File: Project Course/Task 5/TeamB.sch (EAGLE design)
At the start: 33 parts, among them Q1 MIC29300-5.0WU, Q2 MIC29300-3.3WU, Q3 MIC29300-12WU, U0 26V, U1 26V, U2 5V, U3 3.3V, U4 12V

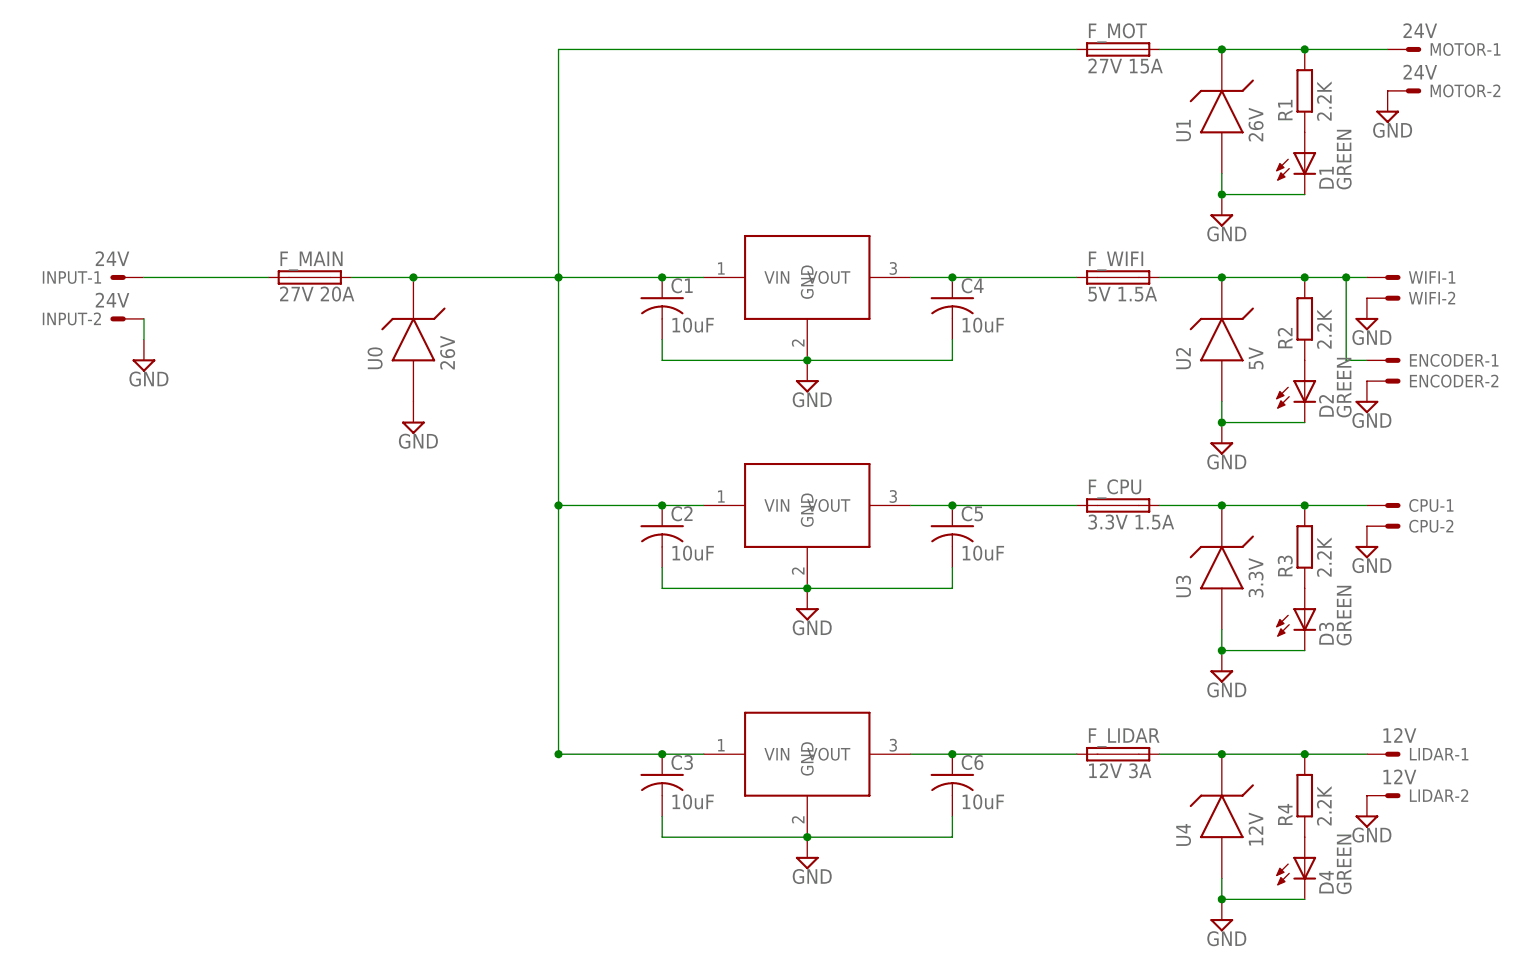
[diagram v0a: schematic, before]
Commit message: Corrected Packages, Verified Trace widths
Used TE5 fuses, and verified everything using 1 oz copper
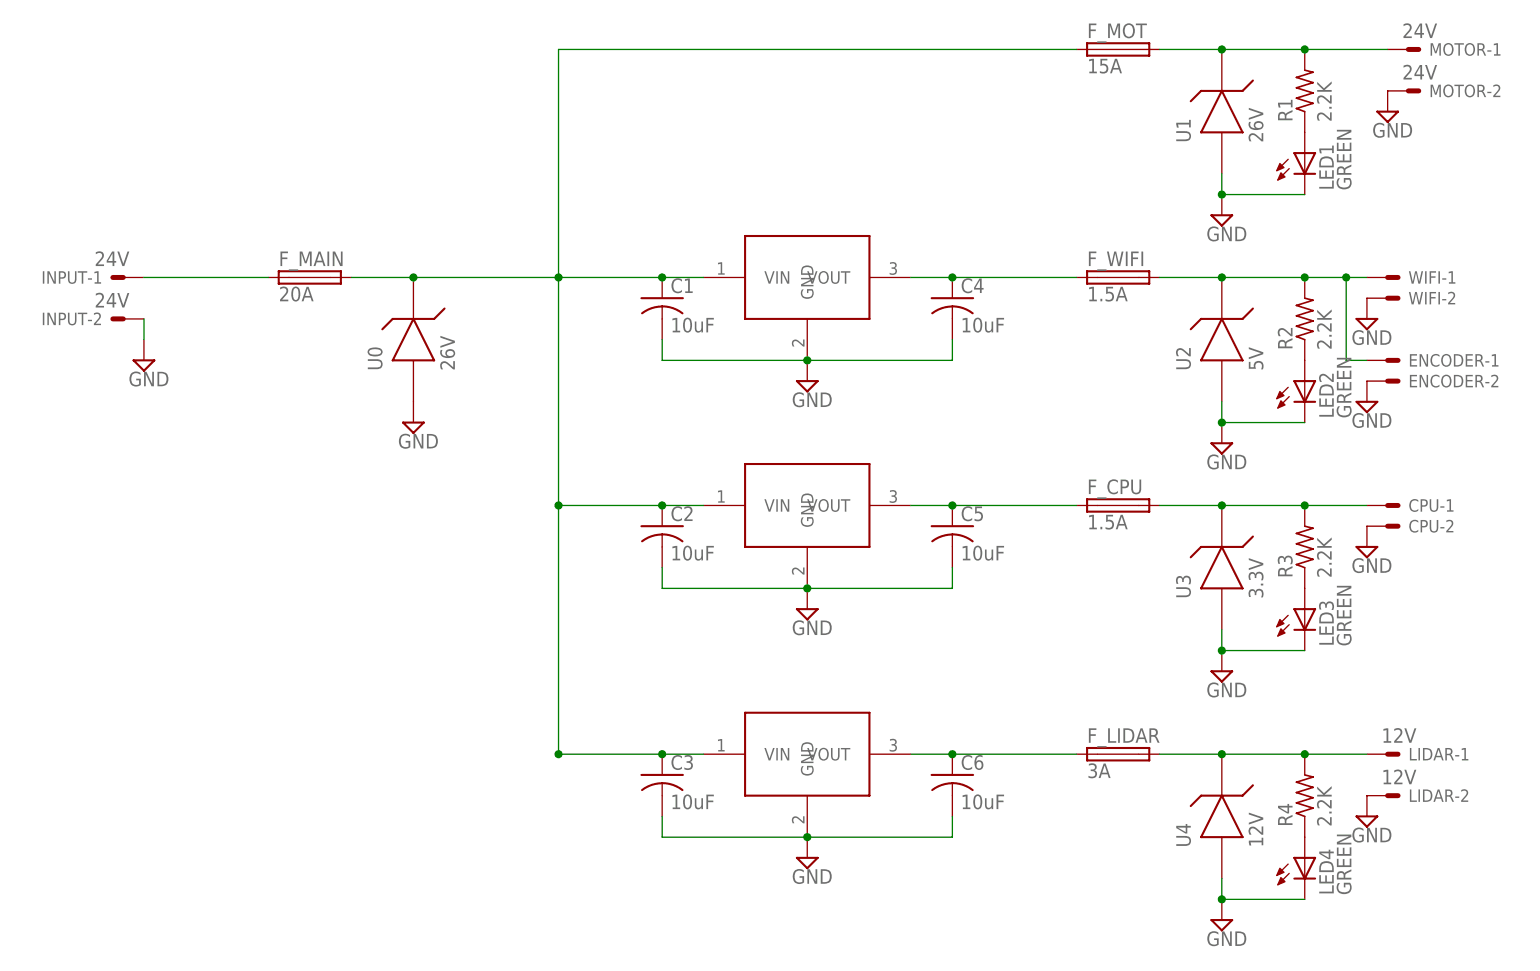
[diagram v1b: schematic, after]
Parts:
- removed D1, D2, D3, D4: GREEN, led:LEDCHIP-LED0805
- added LED1, LED2, LED3, LED4: GREEN, led:LEDSML1206
- C1, C2, C3, C4, C5, C6: device TinyGadget(1):CAPACITORTH_CAP -> rcl:C-USC1206
- F_CPU: value 3.3V 1.5A -> 1.5A
- F_LIDAR: value 12V 3A -> 3A
- F_MAIN: value 27V 20A -> 20A
- F_MOT: value 27V 15A -> 15A
- F_WIFI: value 5V 1.5A -> 1.5A
- R1, R2, R3, R4: device resistor:R-EU_R0402 -> rcl:R-US_R1206
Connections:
- net GND: now also LED1.C, LED2.C, LED3.C, LED4.C; no longer D1.C, D2.C, D3.C, D4.C
- net N$11: now also LED3.A, R3.1; no longer D2.A, R2.1
- net N$13: now also LED4.A; no longer D4.A
- net N$5: now also LED1.A; no longer D1.A
- net N$8: now also LED2.A, R2.1; no longer D3.A, R3.1
